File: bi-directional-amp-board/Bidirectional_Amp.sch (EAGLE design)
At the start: 129 parts, among them J1 73415-2061, J10 73415-2061, J11 73415-2061, J12 73415-2061, J2 73415-2061, J3 22-23-2071, J4 73415-2061, J5 73415-2061, J6 73415-2061, J7 73415-2061, J8 73415-2061, J9 22-23-2031, U1 LTC5536, U10 NC7S32M5X, U11 SN74LV1T34DBVR, U2 LTC6994-1, U3 LTC6994-1, U4 QPC1022, U5 NC7S04M5, U6 TQP9111, U7 TQP3M9035, U8 QPC1022, U9 LTC3428EDDPBF

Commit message: more progress on board
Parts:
- added R39: 100, oresat-rcl:R-US_0603-C-NOSILK
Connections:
- net N$5: now also R39.1
- net PWR_DIV_OUT2: now also R39.2
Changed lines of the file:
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@@
 <layer number="1" name="Top" color="4" fill="1" visible="no" active="no"/>
 <layer number="2" name="Route2" color="1" fill="3" visible="no" active="no"/>
+<layer number="3" name="Route3" color="4" fill="3" visible="no" active="no"/>
+<layer number="4" name="Route4" color="1" fill="4" visible="no" active="no"/>
+<layer number="5" name="Route5" color="4" fill="4" visible="no" active="no"/>
+<layer number="6" name="Route6" color="1" fill="8" visible="no" active="no"/>
+<layer number="7" name="Route7" color="4" fill="8" visible="no" active="no"/>
+<layer number="8" name="Route8" color="1" fill="2" visible="no" active="no"/>
+<layer number="9" name="Route9" color="4" fill="2" visible="no" active="no"/>
+<layer number="10" name="Route10" color="1" fill="7" visible="no" active="no"/>
+<layer number="11" name="Route11" color="4" fill="7" visible="no" active="no"/>
+<layer number="12" name="Route12" color="1" fill="5" visible="no" active="no"/>
+<layer number="13" name="Route13" color="4" fill="5" visible="no" active="no"/>
+<layer number="14" name="Route14" color="1" fill="6" visible="no" active="no"/>
 <layer number="15" name="Route15" color="4" fill="6" visible="no" active="no"/>
 <layer number="16" name="Bottom" color="1" fill="1" visible="no" active="no"/>
@@
 <part name="H3" library="SparkFun-Hardware" library_urn="urn:adsk.eagle:library:519" deviceset="STAND-OFF" device="TIGHT" package3d_urn="urn:adsk.eagle:package:38629/1"/>
 <part name="H4" library="SparkFun-Hardware" library_urn="urn:adsk.eagle:library:519" deviceset="STAND-OFF" device="TIGHT" package3d_urn="urn:adsk.eagle:package:38629/1"/>
+<part name="R39" library="oresat-rcl" deviceset="R-US_" device="0603-C-NOSILK" value="100"/>
 </parts>
 <sheets>
@@
 <instance part="H3" gate="G$1" x="134.62" y="25.4"/>
 <instance part="H4" gate="G$1" x="134.62" y="22.86"/>
+<instance part="R39" gate="R" x="71.12" y="185.42" rot="R90"/>
 </instances>
 <busses>
@@
 <pinref part="PD1" gate="PD" pin="OUT1"/>
 <wire x1="62.23" y1="185.42" x2="66.04" y2="185.42" width="0.1524" layer="91"/>
-<wire x1="66.04" y1="185.42" x2="66.04" y2="165.1" width="0.1524" layer="91"/>
+<wire x1="66.04" y1="185.42" x2="66.04" y2="180.34" width="0.1524" layer="91"/>
+<wire x1="66.04" y1="180.34" x2="66.04" y2="165.1" width="0.1524" layer="91"/>
 <wire x1="66.04" y1="165.1" x2="20.32" y2="165.1" width="0.1524" layer="91"/>
 <wire x1="20.32" y1="165.1" x2="20.32" y2="137.16" width="0.1524" layer="91"/>
+<pinref part="R39" gate="R" pin="1"/>
+<wire x1="71.12" y1="180.34" x2="66.04" y2="180.34" width="0.1524" layer="91"/>
+<junction x="66.04" y="180.34"/>
 </segment>
 </net>
@@
 <segment>
 <pinref part="PD1" gate="PD" pin="OUT2"/>
-<wire x1="62.23" y1="193.04" x2="158.75" y2="193.04" width="0.1524" layer="91"/>
+<wire x1="62.23" y1="193.04" x2="71.12" y2="193.04" width="0.1524" layer="91"/>
 <label x="157.48" y="193.04" size="1.778" layer="95" rot="MR180" xref="yes"/>
+<pinref part="R39" gate="R" pin="2"/>
+<wire x1="71.12" y1="193.04" x2="158.75" y2="193.04" width="0.1524" layer="91"/>
+<wire x1="71.12" y1="190.5" x2="71.12" y2="193.04" width="0.1524" layer="91"/>
+<junction x="71.12" y="193.04"/>
 </segment>
 </net>
@@
 <text x="105.41" y="104.14" size="1.778" layer="97">0402</text>
 <text x="105.41" y="85.09" size="2.54" layer="97">TX/RX Switch 1</text>
-<text x="27.94" y="135.89" size="1.778" layer="97">Inverter U5 causes TX/RX Switch 1
+<text x="20.32" y="135.89" size="1.778" layer="97">Inverter U5 causes TX/RX Switch 1
 to select RF2 port during transmit.
 TX/RX Switch 2, without inverter,

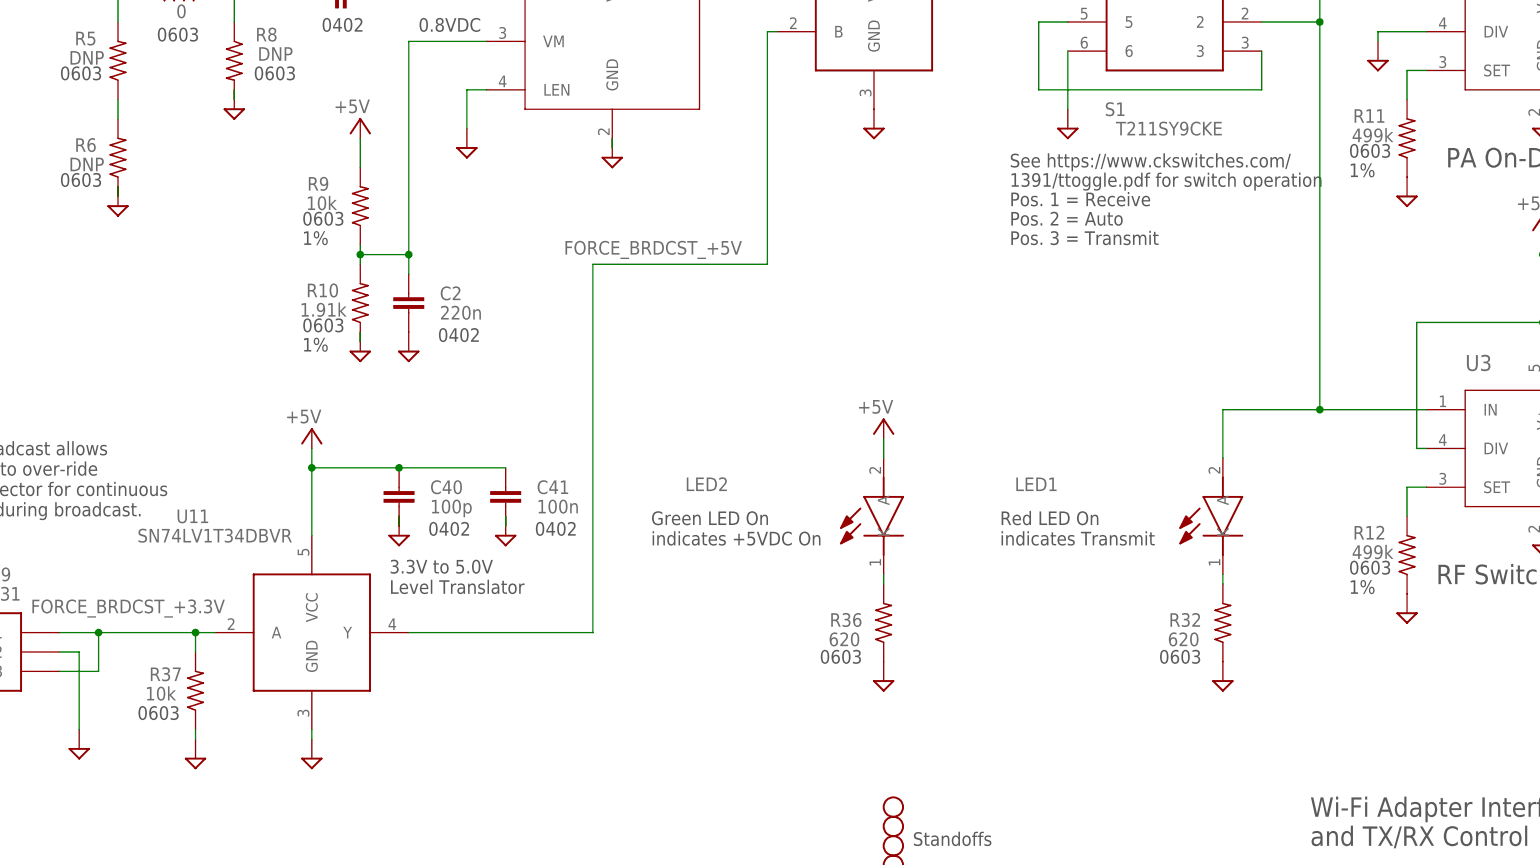
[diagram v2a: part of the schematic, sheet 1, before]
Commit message: Change to 0402 for some Resistors
Changed resistors from 0603 to 0402 when electrically OK
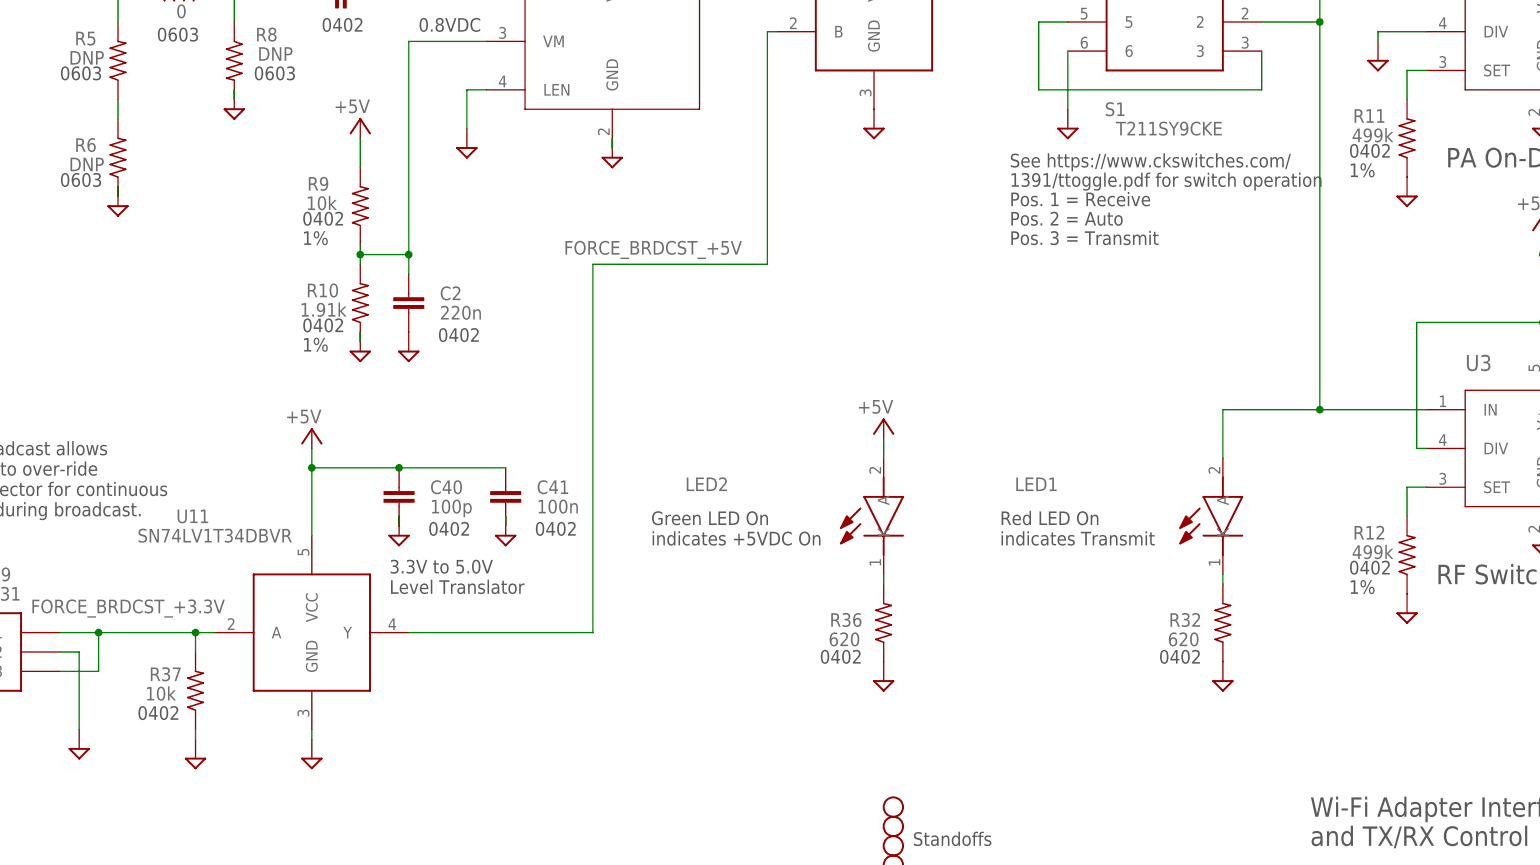
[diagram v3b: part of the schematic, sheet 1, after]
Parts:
- R10: device rcl:R-US_R0603 -> oresat-rcl:R-US_0402-B-NOSILK; MPN ERJ-3EKF1911V -> ERJ-2RKF1911X
- R11, R12: device rcl:R-US_R0603 -> oresat-rcl:R-US_0402-B-NOSILK; MPN CRCW0603499KFKEB -> ERJ-2RKF4993X
- R13, R15, R24, R26, R30: device rcl_custom:R-US_0603-B-NOSILK -> oresat-rcl:R-US_0402-B-NOSILK; MPN ERJ-3EKF1002V -> ERJ-2RKF1002X
- R14, R16, R25, R27: device rcl_custom:R-US_0603-B-NOSILK -> oresat-rcl:R-US_0402-B-NOSILK; MPN ERJ-3EKF5621V -> ERJ-2RKF5621X
- R21, R9: device rcl:R-US_R0603 -> oresat-rcl:R-US_0402-B-NOSILK; MPN ERJ-3EKF1002V -> ERJ-2RKF1002X
- R22: device rcl:R-US_R0603 -> oresat-rcl:R-US_0402-B-NOSILK; MPN ERJ-3GEYJ333V -> ERJ-2GEJ333X
- R28: device rcl_custom:R-US_0603-B-NOSILK -> oresat-rcl:R-US_0402-B-NOSILK; MPN ERJ-3EKF3833V -> ERJ-2RKF3833X
- R29: device rcl_custom:R-US_0603-B-NOSILK -> oresat-rcl:R-US_0402-B-NOSILK; MPN ERJ-3EKF1213V -> ERJ-2RKF1213X
- R31, R37: device rcl_custom:R-US_0603-B-NOSILK -> oresat-rcl:R-US_0402-B-NOSILK; MPN ERJ-3GEYJ103V -> ERJ-2GEJ103X
- R32, R36: device rcl:R-US_R0603 -> oresat-rcl:R-US_0402-B-NOSILK; MPN ERJ-3GEYJ621V -> ERJ-2GEJ621X
- R35: device oresat-rcl:R-US_0402-A -> oresat-rcl:R-US_0402-B-NOSILK
- R39: MPN (none) -> ERJ-3EKF1000V

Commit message: more progress on board
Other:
- moved on the sheet: U6
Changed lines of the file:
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@@
 <?xml version="1.0" encoding="utf-8"?>
 <!DOCTYPE eagle SYSTEM "eagle.dtd">
-<eagle version="9.1.1">
+<eagle version="9.1.2">
 <drawing>
 <settings>
-<setting alwaysvectorfont="no"/>
+<setting alwaysvectorfont="yes"/>
 <setting verticaltext="up"/>
 </settings>
@@
 <class number="0" name="default" width="0" drill="0">
 </class>
-<class number="1" name="RF" width="0.3302" drill="0">
-<clearance class="1" value="0.75"/>
+<class number="1" name="RF" width="0" drill="0">
+<clearance class="0" value="0.75"/>
+</class>
+<class number="2" name="pad_rf" width="0" drill="0">
+<clearance class="0" value="0.75"/>
 </class>
 </classes>
@@
 </segment>
 </net>
-<net name="N$23" class="1">
+<net name="N$23" class="2">
 <segment>
 <pinref part="U6" gate="U" pin="RFIN@4"/>

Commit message: still mroe progress on board
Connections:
- removed net N$23: R18.2, U6.RFIN@2, U6.RFIN@3, U6.RFIN@4
- new net N$56: R18.2, U6.RFIN
- net N$24: now also U6.RFOUT; no longer U6.RFOUT@12, U6.RFOUT@13, U6.RFOUT@14
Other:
- moved on the sheet: C18, C20, C21, C22, C23, C24, L1, L3, R17, R18, R19, R20

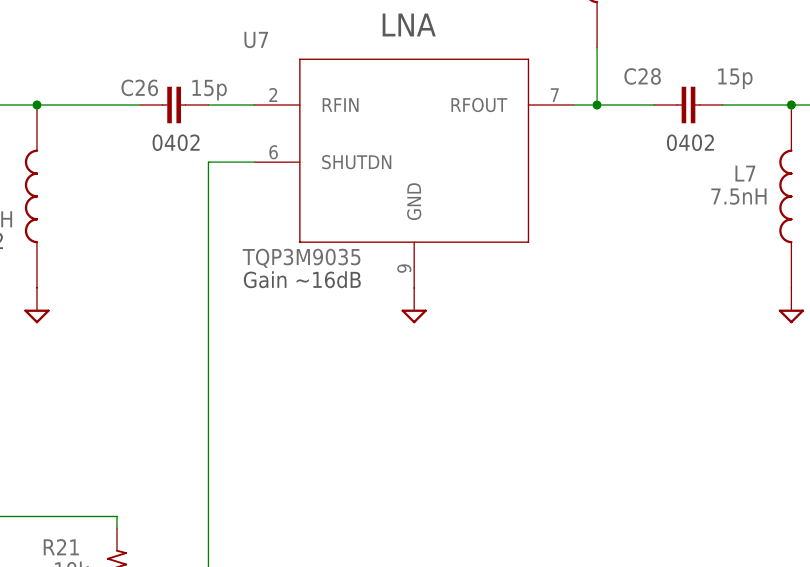
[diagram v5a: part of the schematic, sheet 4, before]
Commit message: mostly finished rough layout of wifi board
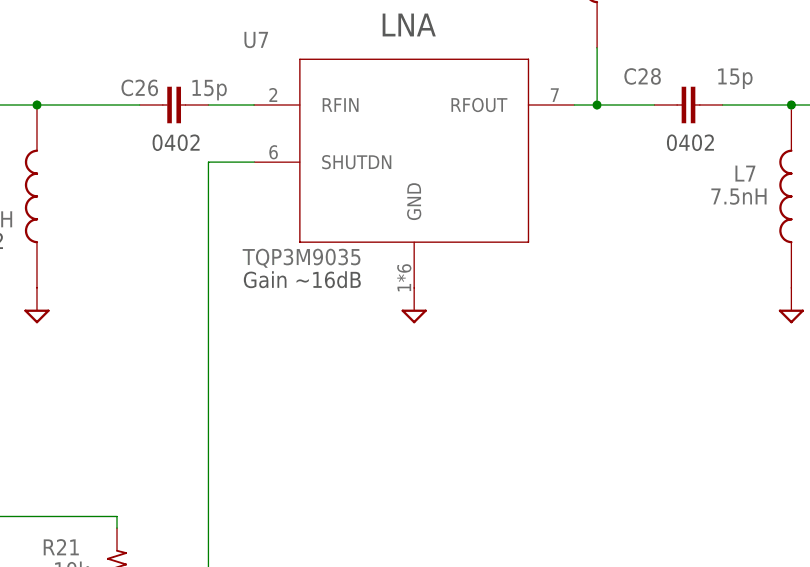
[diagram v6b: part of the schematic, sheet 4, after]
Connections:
- net N$36 renamed SWA
- net N$37 renamed SWB
- net N$38 renamed VOUT
- net N$39 renamed FB
- net N$42 renamed SHDN
- net N$43 renamed VC
- net N$44 renamed VIN
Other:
- moved on the sheet: U7
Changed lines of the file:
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@@
 </segment>
 </net>
-<net name="N$36" class="0">
+<net name="SWA" class="0">
 <segment>
 <pinref part="L9" gate="G$1" pin="1"/>
@@
 </segment>
 </net>
-<net name="N$37" class="0">
+<net name="SWB" class="0">
 <segment>
 <pinref part="L10" gate="G$1" pin="1"/>
@@
 </segment>
 </net>
-<net name="N$38" class="0">
+<net name="VOUT" class="0">
 <segment>
 <pinref part="U9" gate="A" pin="VOUT"/>
@@
 </segment>
 </net>
-<net name="N$39" class="0">
+<net name="FB" class="0">
 <segment>
 <pinref part="U9" gate="A" pin="FB"/>
@@
 </segment>
 </net>
-<net name="N$42" class="0">
+<net name="SHDN" class="0">
 <segment>
 <pinref part="U9" gate="A" pin="!SHDN"/>
@@
 </segment>
 </net>
-<net name="N$43" class="0">
+<net name="VC" class="0">
 <segment>
 <pinref part="U9" gate="A" pin="VC"/>
@@
 </segment>
 </net>
-<net name="N$44" class="0">
+<net name="VIN" class="0">
 <segment>
 <pinref part="L10" gate="G$1" pin="2"/>

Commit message: lots of progress on wifi board
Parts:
- added C43: 4.7uF, rcl:C-EUC1206
- added C44: 1000pF, rcl:C-EUC0603
- added C45: 22pF, rcl:C-EUC0402
- added C46, C47: 22uF, rcl:C-EUC1210
- added D3, D4: DIODE-SCHOTTKY-PMEG4005EJ, SparkFun-DiscreteSemi:DIODE-SCHOTTKY-PMEG4005EJ
- added J13: 22-23-2071, 22-23-2071:22-23-2071
- added L13, L14: 2.2uH, SamacSys_Parts:XFL4020-222MEB
- added R40: 383k, oresat-rcl:R-US_0402-B-NOSILK
- added R41: 121k, oresat-rcl:R-US_0402-B-NOSILK
- added R42, R43: 10k, oresat-rcl:R-US_0402-B-NOSILK
- added U12: LTC3428EDDPBF, LTC3428:LTC3428EDDPBF
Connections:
- new net FB1: R40.1, R41.2, U12.FB
- new net N$23: C44.1, R42.1
- new net N$36: C47.1, J13-3.S
- new net SHDN1: J13-7.S, R43.1, U12.!SHDN
- new net SWA1: D3.A, L13.1, U12.SWA
- new net SWB1: D4.A, L14.1, U12.SWB
- new net VC1: C45.1, R42.2, U12.VC
- new net VIN1: C43.1, J13-6.S, L13.2, L14.2, R43.2, U12.VIN
- new net VOUT1: C46.1, D3.C, D4.C, J13-5.S, R40.2, U12.VOUT
- net +5V: now also J13-4.S
- net GND: now also C43.2, C44.2, C45.2, C46.2, C47.2, J13-1.S, J13-2.S, R41.1, U12.GND@1, U12.GND@10, U12.GND@11, U12.GND@7
